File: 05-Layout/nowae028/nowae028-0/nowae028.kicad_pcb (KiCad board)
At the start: 2 copper layers, 25.4 x 36.8 mm, 10 parts, among them J1 JUMPER-2, J2 JUMPER-2, P1 CONN, U1 AMW037

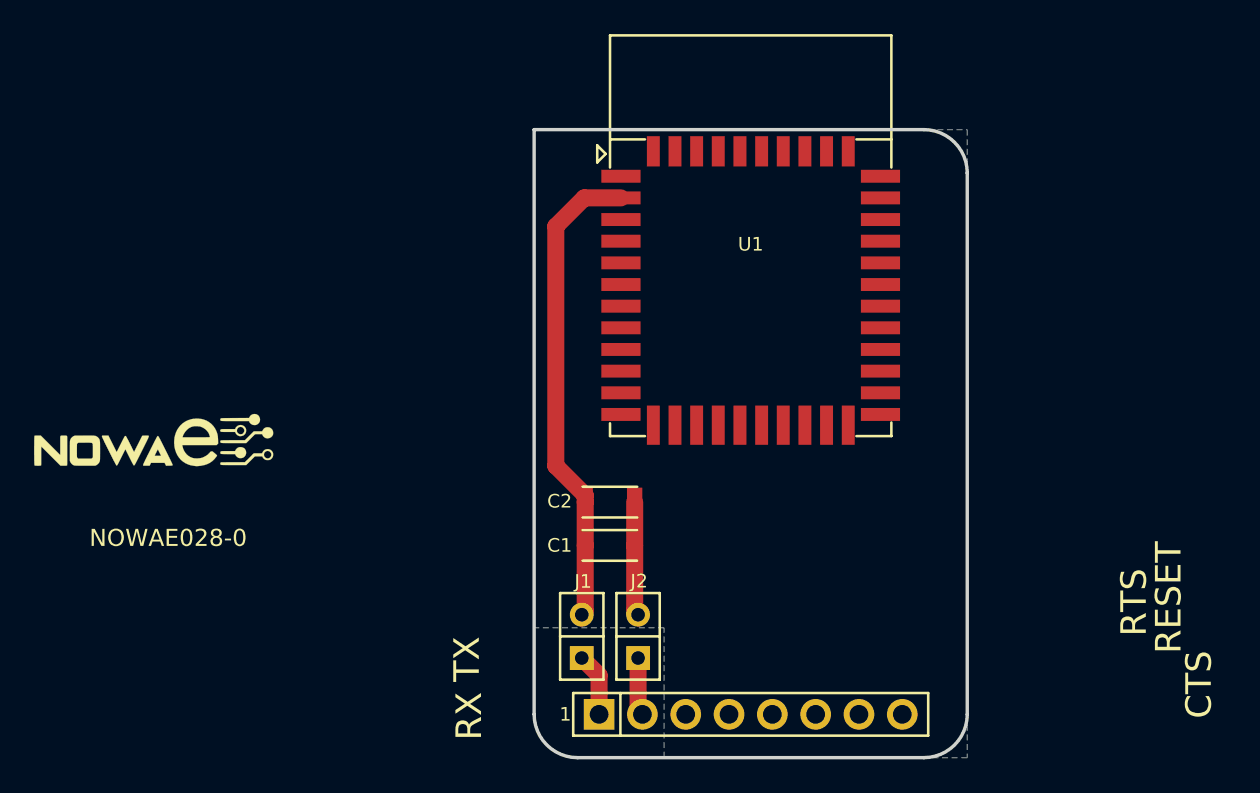
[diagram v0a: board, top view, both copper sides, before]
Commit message: Ended PCB: fixed silkscreen, net, and ground plane (nowae028)
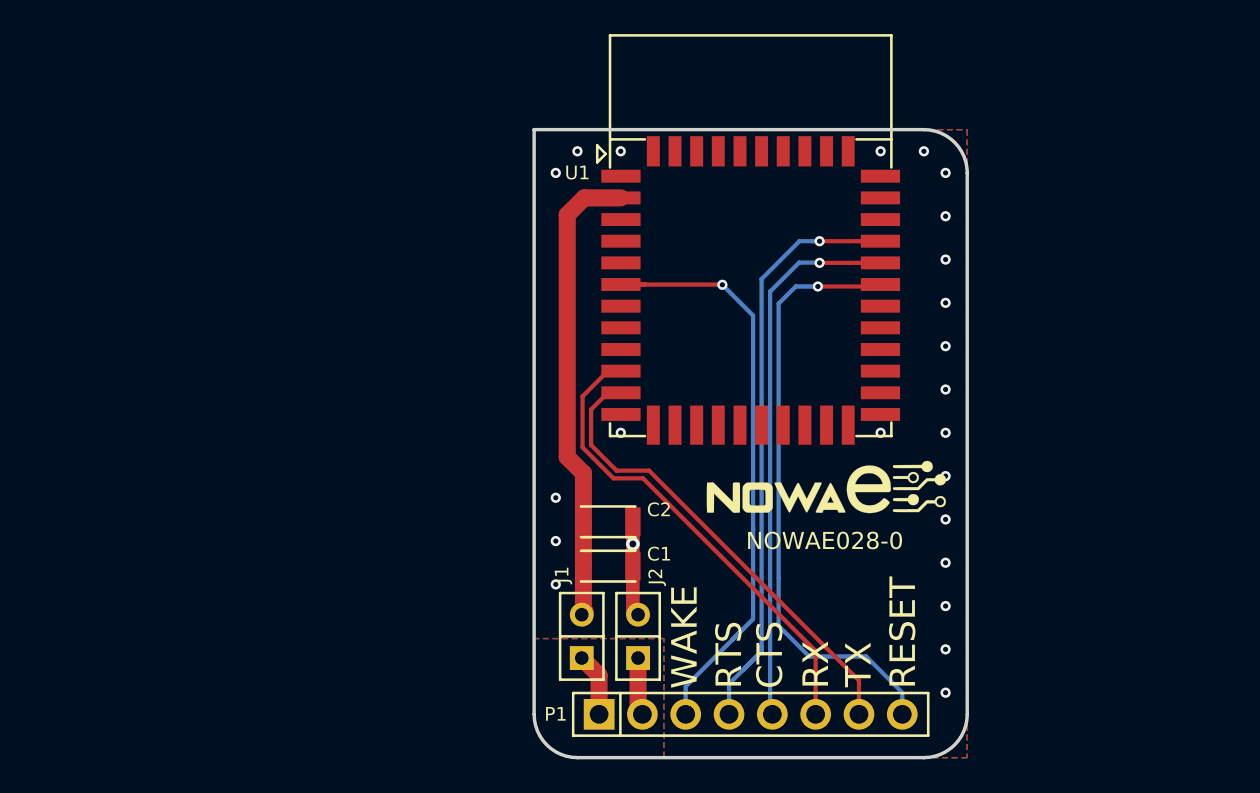
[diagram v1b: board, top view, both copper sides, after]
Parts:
- moved G*** 49.1 mm to (154.9, 90.2)
- moved G*** 39.5 mm to (153.0, 85.7)
- moved G*** 39.0 mm to (142.2, 88.9)
- moved G*** 35.1 mm to (148.6, 77.6)
- moved C1 1.22 mm to (140.2, 90.4)
- moved C2 1.16 mm to (140.2, 87.8)
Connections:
- P1 pad 3: /WIFI_RESET -> /WIFI_WAKE
- P1 pad 8: /WIFI_WAKE -> /WIFI_RESET
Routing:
- net /WIFI_WAKE: track 0.00 -> 36.0 mm, vias 0 -> 1
- net /WIFI_RTS: track 0.00 -> 35.7 mm, vias 0 -> 1
- net /WIFI_RESET: track 0.00 -> 35.5 mm, vias 0 -> 1
- net /WIFI_CTS: track 0.00 -> 32.0 mm, vias 0 -> 1
- net /WIFI_RX: track 0.00 -> 28.2 mm
- net /WIFI_TX: track 0.00 -> 27.7 mm
- net GND-ISO: track 6.69 -> 5.86 mm, vias 0 -> 24
- added copper zone on F.Cu, net GND-ISO
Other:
- board text added: "WAKE"
